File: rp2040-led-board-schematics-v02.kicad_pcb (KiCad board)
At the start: 4 copper layers, 153.7 x 82.5 mm, 117 parts, among them J1 GPIO, J10 LED1Terminal, J11 MainBoard, J12 FrontPanel, J14 ReceiverData, J15 ReceiverRS485, J2 PWR_IN, J3 LED1Terminal, J4 LED1Terminal, J5 LED1Terminal, J6 LED1Terminal, J7 LED1Terminal, J8 LED1Terminal, J9 LED1Terminal, SW1 Button, SW2 PEC16, U1 Pico, U10 MAX485E, U11 LM7805, U12 MAX485E, U14 LM7805, U2 ENC28J60, U3 MAX485E, U4 MAX485E, U5 MAX485E, U6 MAX485E, U7 MAX485E, U8 MAX485E, U9 MAX485E

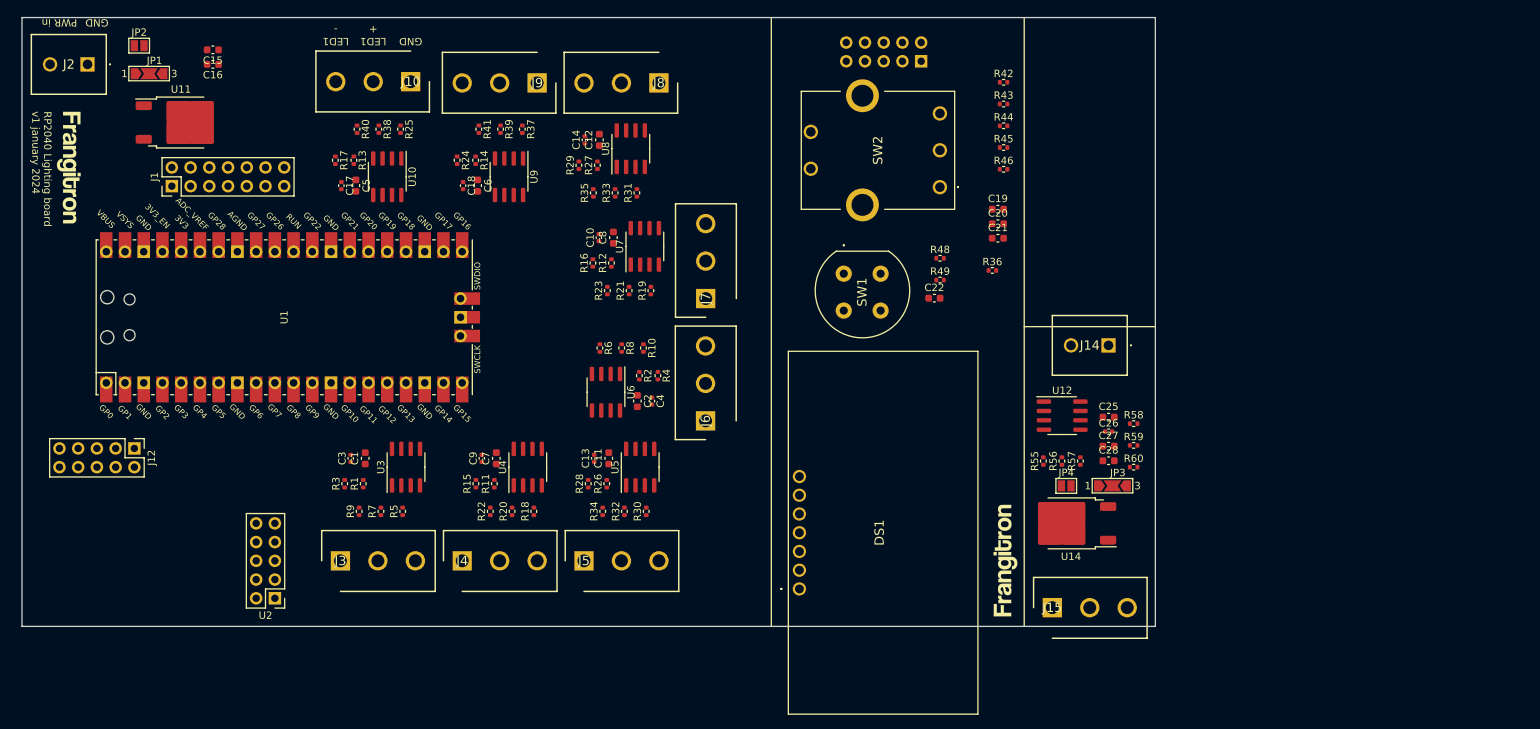
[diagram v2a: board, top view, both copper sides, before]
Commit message: main board PCB done (needs checking)
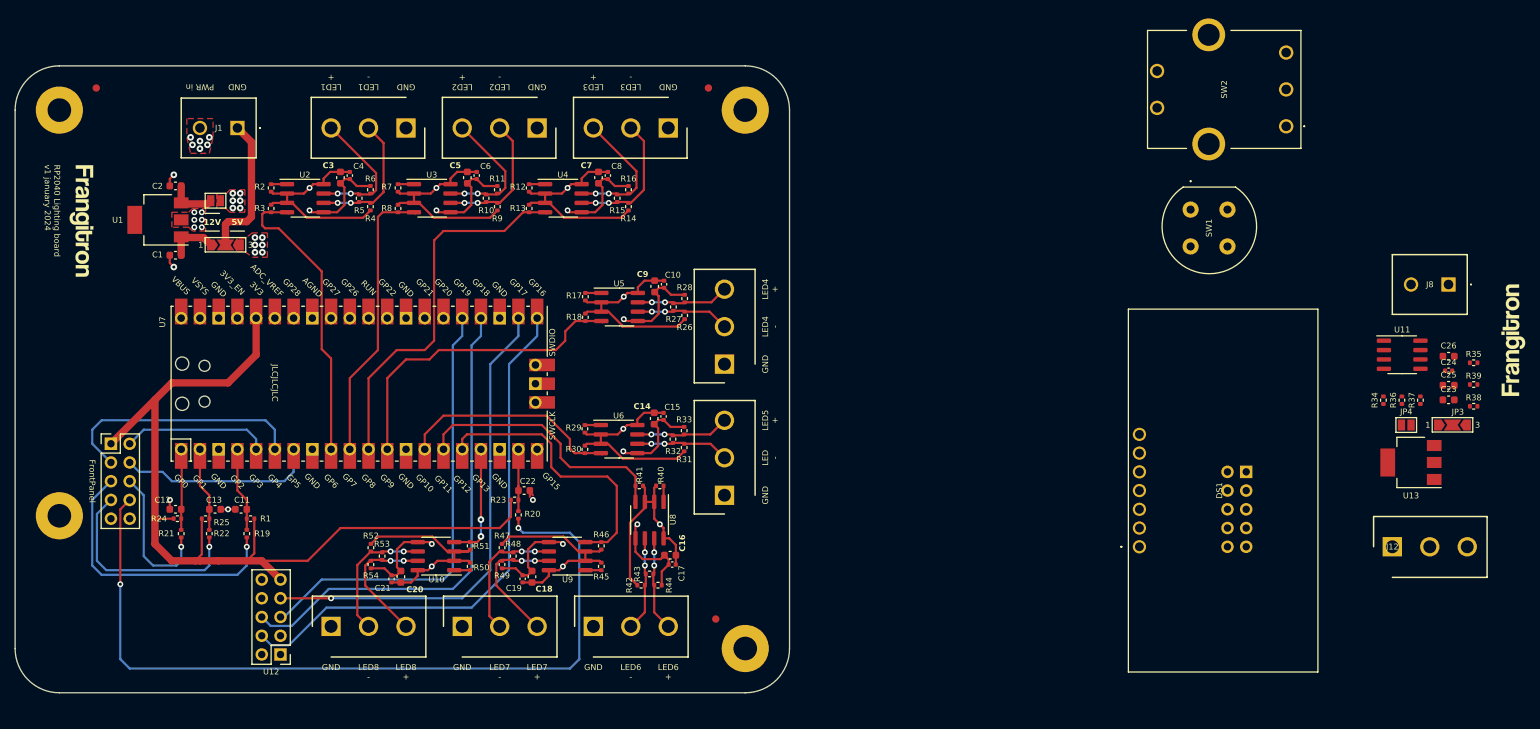
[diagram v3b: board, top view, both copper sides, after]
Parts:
- removed the J1 at (95.2, 67.3)
- removed J10, J3, J4, J6, J7, J9: LED1Terminal, Frangitron:ScrewTerminal_01x03_5.08_Amphenol
- removed the J5 at (151.1, 118.1)
- removed the J8 at (161.3, 53.3)
- removed the U1 at (110.5, 85.1)
- added FM1: Fiducial, Fiducial:Fiducial_1mm_Mask2mm, F.Cu at (85.0, 54.0)
- added FM2: Fiducial, Fiducial:Fiducial_1mm_Mask2mm, F.Cu at (168.0, 54.0)
- added FM3: Fiducial, Fiducial:Fiducial_1mm_Mask2mm, F.Cu at (169.0, 126.0)
- added H1: MountingHole_Pad, MountingHole:MountingHole_3.2mm_M3_Pad, F.Cu at (80.0, 57.0)
- added H2: MountingHole_Pad, MountingHole:MountingHole_3.2mm_M3_Pad, F.Cu at (173.0, 57.0)
- added H4: MountingHole_Pad, MountingHole:MountingHole_3.2mm_M3_Pad, F.Cu at (80.0, 112.0)
- added H5: MountingHole_Pad, MountingHole:MountingHole_3.2mm_M3_Pad, F.Cu at (173.0, 130.0)
- added J14: Terminal, Frangitron:ScrewTerminal_01x03_5.08_Amphenol, F.Cu at (144.8, 59.4)
- added J15: Terminal, Frangitron:ScrewTerminal_01x03_5.08_Amphenol, F.Cu at (162.6, 59.4)
- added J16: Terminal, Frangitron:ScrewTerminal_01x03_5.08_Amphenol, F.Cu at (170.2, 91.4)
- added J17: Terminal, Frangitron:ScrewTerminal_01x03_5.08_Amphenol, F.Cu at (170.2, 109.2)
- added J18: Terminal, Frangitron:ScrewTerminal_01x03_5.08_Amphenol, F.Cu at (152.4, 127.0)
- added J19: Terminal, Frangitron:ScrewTerminal_01x03_5.08_Amphenol, F.Cu at (134.6, 127.0)
- added J2: Terminal, Frangitron:ScrewTerminal_01x03_5.08_Amphenol, F.Cu at (127.0, 59.4)
- added J20: Terminal, Frangitron:ScrewTerminal_01x03_5.08_Amphenol, F.Cu at (116.8, 127.0)
- added U7: Pico, MCU_RaspberryPi_and_Boards:RPi_Pico_SMD_TH, F.Cu at (120.7, 94.1)
- C14: renamed from C9; value 10uF -> 100nF; footprint Capacitor_SMD:C_0402_1005Metric -> Capacitor_SMD:C_0603_1608Metric
- C17: renamed from C7; value 100nF -> 10uF; footprint Capacitor_SMD:C_0603_1608Metric -> Capacitor_SMD:C_0402_1005Metric
- C18: renamed from C4; value 10uF -> 100nF; footprint Capacitor_SMD:C_0402_1005Metric -> Capacitor_SMD:C_0603_1608Metric
- C19: renamed from C2; value 100nF -> 10uF; footprint Capacitor_SMD:C_0603_1608Metric -> Capacitor_SMD:C_0402_1005Metric
- C7: renamed from C10; value 10uF -> 100nF; footprint Capacitor_SMD:C_0402_1005Metric -> Capacitor_SMD:C_0603_1608Metric
- C8: value 100nF -> 10uF; footprint Capacitor_SMD:C_0603_1608Metric -> Capacitor_SMD:C_0402_1005Metric
- R11: renamed from R12; value 10K -> 20K
- R13: renamed from R39; value 20K -> 10K
- R14: renamed from R27; value 10K -> 20K
- R15: renamed from R33; value 20K -> 120
- R18: renamed from R31; value 20K -> 10K
- R2: renamed from R40; value 120 -> 10K
- R22: renamed from R44; value 10k -> 1k
- R25: renamed from R36; value 1k -> 10k
- R27: renamed from R2; value 10K -> 120
- R28: renamed from R23; value 120 -> 20K
- R30: renamed from R8; value 20K -> 10K
- R32: renamed from R6; value 20K -> 120
- R33: renamed from R10; value 120 -> 20K
- R4: renamed from R17; value 10K -> 20K
- R40: renamed from R7; value 20K -> 10K
- R41: renamed from R9; value 120 -> 10K
- R43: renamed from R15; value 10K -> 120
- R44: renamed from R3; value 10K -> 20K
- R45: renamed from R22; value 120 -> 10K
- R47: renamed from R34; value 120 -> 20K
- R48: renamed from R32; value 20K -> 120
- R5: renamed from R25; value 20K -> 120
- R50: renamed from R30; value 20K -> 10K
- R52: renamed from R26; value 10K -> 20K
- R53: renamed from R18; value 20K -> 120
- R54: renamed from R11; value 10K -> 20K
- R6: renamed from R24; value 10K -> 20K
- R7: renamed from R38; value 20K -> 10K
- R9: renamed from R41; value 120 -> 20K
- U1: renamed from U11; footprint Package_TO_SOT_SMD:TO-252-2 -> Package_TO_SOT_SMD:SOT-223
- U13: renamed from U14; footprint Package_TO_SOT_SMD:TO-252-2 -> Package_TO_SOT_SMD:SOT-223
- moved R24 125.3 mm to (96.0, 112.4)
- moved R21 123.2 mm to (96.5, 114.4), turned to -90 degrees
- moved R22 121.1 mm to (100.3, 114.4), turned to -90 degrees
- moved C12 118.0 mm to (95.7, 111.1), turned to 180 degrees
- moved R1 118.0 mm to (105.9, 112.4), turned to 180 degrees
- moved R19 113.9 mm to (105.4, 114.4), turned to 90 degrees
- moved C13 112.3 mm to (101.1, 111.1)
- moved R25 111.9 mm to (99.8, 112.4)
- moved C11 110.4 mm to (104.6, 111.1), turned to 180 degrees
- moved H6 75.1 mm to (277.1, 88.2)
- moved J13 71.0 mm to (240.9, 106.0), turned to 180 degrees
- moved R20 66.9 mm to (142.2, 111.9), turned to -90 degrees
- moved R23 64.9 mm to (141.7, 109.9)
- moved C22 61.4 mm to (143.0, 108.6)
- moved SW1 47.8 mm to (233.4, 70.5)
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- renumbered C15 to C1, C14 to C10, C19 to C11, C20 to C12, C21 to C13, C3 to C15, C1 to C16, C16 to C2, C11 to C20, C13 to C21, C28 to C23, C26 to C24, C27 to C25, C25 to C26, C6 to C3, C17 to C4, C18 to C6, C12 to C9, H1 to H3, H2 to H6, H4 to H7, J2 to J1, J15 to J12, J11 to J13, J12 to J5, J14 to J8, JP2 to JP1, JP1 to JP2, R42 to R1, R35 to R10, R16 to R12, R37 to R16, R29 to R17, R46 to R19, R48 to R20, R45 to R21, R49 to R23, R43 to R24, R19 to R26, R4 to R29, R13 to R3, R21 to R31, R55 to R34, R58 to R35, R56 to R36, R57 to R37, R60 to R38, R59 to R39, R5 to R42, R1 to R46, R20 to R49, R28 to R51, R14 to R8, U5 to U10, U12 to U11, U2 to U12, U10 to U2, U8 to U3, U7 to U4, U9 to U5, U3 to U6, U6 to U8, U4 to U9
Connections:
- C11 pad 1: FPEncoderA -> MCUEncoderS
- C12 pad 1: FPEncoderB -> MCUEncoderA
- C13 pad 1: FPEncoderS -> MCUEncoderB
- C22 pad 1: FPSwitchPush -> MCUSwitchPush
- DS1 pad 1: GND -> FP GND
- DS1 pad 2: +3V3 -> FP +3V3
- DS1 pad 3: +3V3 -> FP +3V3
- DS1 pad 4: GND -> FP GND
- J13 pad 1: +3V3 -> FP +3V3
- J13 pad 10: GND -> FP GND
- J5 pad 2: MBDisplayRST -> MCUDisplayRST
- J5 pad 3: MBDisplaySDA -> MCUDisplaySDA
- J5 pad 4: MBDisplaySCL -> MCUDisplaySCL
- R1 pad 2: FPEncoderA -> MCUEncoderS
- R10 pad 1: Net-(J8-Pin_3) -> /LED to RS486/D+
- R10 pad 2: Net-(J8-Pin_2) (its old number) -> /LED to RS486/D-
- R11 pad 1: +5V -> /LED to RS486/D+
- R11 pad 2: Net-(U7-RO) -> GND
- R12 pad 2: LED5 out -> Net-(U4-RO)
- R13 pad 1: Net-(J9-Pin_3) -> +5V
- R13 pad 2: GND -> LED3 out
- R14 pad 2: Net-(U8-RO) -> /LED to RS487/D-
- R15 pad 1: Net-(J8-Pin_3) -> /LED to RS487/D+
- R15 pad 2: GND -> /LED to RS487/D-
- R16 pad 1: +5V -> /LED to RS487/D+
- R16 pad 2: Net-(J9-Pin_2) -> GND
- R17 pad 2: LED6 out -> Net-(U5-RO)
- R18 pad 2: Net-(J8-Pin_2) (its old number) -> LED4 out
- R19 pad 1: FPEncoderB -> MBEncoderS
- R19 pad 2: Net-(R46-Pad2) -> MCUEncoderS
- R2 pad 1: Net-(J10-Pin_3) -> +5V
- R2 pad 2: Net-(J10-Pin_2) -> Net-(U2-RO)
- R20 pad 1: FPSwitchPush -> MCUSwitchPush
- R20 pad 2: Net-(SW1-K) -> MBSwitchPush
- R21 pad 1: FPEncoderA -> MCUEncoderA
- R21 pad 2: Net-(R45-Pad2) -> MBEncoderA
- R22 pad 1: +3V3 -> MCUEncoderB
- R22 pad 2: FPEncoderS -> MBEncoderB
- R23 pad 2: FPSwitchPush -> MCUSwitchPush
- R24 pad 2: FPEncoderB -> MCUEncoderA
- R25 pad 1: Net-(R36-Pad1) -> +3V3
- R25 pad 2: FPEncoderS -> MCUEncoderB
- R26 pad 2: Net-(J7-Pin_2) -> /LED to RS488/D-
- R27 pad 1: +5V -> /LED to RS488/D+
- R27 pad 2: Net-(U6-RO) -> /LED to RS488/D-
- R28 pad 1: Net-(J7-Pin_3) -> /LED to RS488/D+
- R28 pad 2: Net-(J7-Pin_2) -> GND
- R29 pad 2: LED4 out -> Net-(U6-RO)
- R3 pad 2: Net-(U10-RO) -> LED1 out
- R30 pad 1: Net-(J6-Pin_3) -> +5V
- R30 pad 2: GND -> LED5 out
- R31 pad 1: Net-(J7-Pin_3) -> +5V
- R31 pad 2: GND -> /LED to RS489/D-
- R32 pad 1: +5V -> /LED to RS489/D+
- R32 pad 2: Net-(J6-Pin_2) -> /LED to RS489/D-
- R33 pad 1: Net-(J6-Pin_3) -> /LED to RS489/D+
- R33 pad 2: Net-(J6-Pin_2) -> GND
- R4 pad 2: LED8 out -> /LED to RS485/D-
- R40 pad 1: Net-(J3-Pin_3) -> +5V
- R40 pad 2: GND -> Net-(U8-RO)
- R41 pad 1: Net-(J3-Pin_3) -> +5V
- R41 pad 2: Net-(J3-Pin_2) -> LED6 out
- R42 pad 2: Net-(J3-Pin_2) -> /LED to RS490/D-
- R43 pad 1: +5V -> /LED to RS490/D+
- R43 pad 2: LED2 out -> /LED to RS490/D-
- R44 pad 1: +5V -> /LED to RS490/D+
- R44 pad 2: LED1 out -> GND
- R45 pad 1: Net-(J4-Pin_3) -> +5V
- R45 pad 2: Net-(J4-Pin_2) -> Net-(U9-RO)
- R46 pad 2: Net-(U3-RO) -> LED7 out
- R47 pad 1: Net-(J5-Pin_3) -> +5V
- R47 pad 2: Net-(J5-Pin_2) -> /LED to RS491/D-
- R48 pad 1: Net-(J5-Pin_3) -> /LED to RS491/D+
- R48 pad 2: GND -> /LED to RS491/D-
- R49 pad 1: Net-(J4-Pin_3) -> /LED to RS491/D+
- R5 pad 1: +5V -> /LED to RS485/D+
- R5 pad 2: Net-(J10-Pin_2) -> /LED to RS485/D-
- R50 pad 2: Net-(J5-Pin_2) -> Net-(U10-RO)
- R51 pad 2: LED3 out -> LED8 out
- R52 pad 2: Net-(U5-RO) -> /LED to RS492/D-
- R53 pad 1: +5V -> /LED to RS492/D+
- R53 pad 2: Net-(J4-Pin_2) -> /LED to RS492/D-
- R54 pad 1: +5V -> /LED to RS492/D+
- R54 pad 2: Net-(U4-RO) -> GND
- R6 pad 1: +5V -> /LED to RS485/D+
- R6 pad 2: LED7 out -> GND
- R7 pad 1: Net-(J10-Pin_3) -> +5V
- R7 pad 2: GND -> Net-(U3-RO)
- R8 pad 2: Net-(U9-RO) -> LED2 out
- R9 pad 1: Net-(J9-Pin_3) -> +5V
- R9 pad 2: Net-(J9-Pin_2) -> /LED to RS486/D-
- SW1 pad 2: GND -> FP GND
- SW1 pad 3: Net-(SW1-K) -> FPSwitchPush
- SW2 pad A1: Net-(R45-Pad2) -> FPEncoderA
- SW2 pad B1: Net-(R46-Pad2) -> FPEncoderB
- SW2 pad C1: GND -> FP GND
- SW2 pad D1: Net-(R36-Pad1) -> FPEncoderS
- SW2 pad E1: GND -> FP GND
- U10 pad 1: Net-(U5-RO) -> Net-(U10-RO)
- U10 pad 4: LED3 out -> LED8 out
- U10 pad 6: Net-(J5-Pin_2) -> /LED to RS492/D-
- U10 pad 7: Net-(J5-Pin_3) -> /LED to RS492/D+
- U2 pad 1: Net-(U10-RO) -> Net-(U2-RO)
- U2 pad 4: LED8 out -> LED1 out
- U2 pad 6: Net-(J10-Pin_2) -> /LED to RS485/D-
- U2 pad 7: Net-(J10-Pin_3) -> /LED to RS485/D+
- U3 pad 1: Net-(U8-RO) -> Net-(U3-RO)
- U3 pad 4: LED6 out -> LED2 out
- U3 pad 6: Net-(J8-Pin_2) (its old number) -> /LED to RS486/D-
- U3 pad 7: Net-(J8-Pin_3) -> /LED to RS486/D+
- U4 pad 1: Net-(U7-RO) -> Net-(U4-RO)
- U4 pad 4: LED5 out -> LED3 out
- U4 pad 6: Net-(J7-Pin_2) -> /LED to RS487/D-
- U4 pad 7: Net-(J7-Pin_3) -> /LED to RS487/D+
- U5 pad 1: Net-(U9-RO) -> Net-(U5-RO)
- U5 pad 4: LED7 out -> LED4 out
- U5 pad 6: Net-(J9-Pin_2) -> /LED to RS488/D-
- U5 pad 7: Net-(J9-Pin_3) -> /LED to RS488/D+
- U6 pad 1: Net-(U3-RO) -> Net-(U6-RO)
- U6 pad 4: LED1 out -> LED5 out
- U6 pad 6: Net-(J3-Pin_2) -> /LED to RS489/D-
- U6 pad 7: Net-(J3-Pin_3) -> /LED to RS489/D+
- U8 pad 1: Net-(U6-RO) -> Net-(U8-RO)
- U8 pad 4: LED4 out -> LED6 out
- U8 pad 6: Net-(J6-Pin_2) -> /LED to RS490/D-
- U8 pad 7: Net-(J6-Pin_3) -> /LED to RS490/D+
- U9 pad 1: Net-(U4-RO) -> Net-(U9-RO)
- U9 pad 4: LED2 out -> LED7 out
- U9 pad 6: Net-(J4-Pin_2) -> /LED to RS491/D-
- U9 pad 7: Net-(J4-Pin_3) -> /LED to RS491/D+
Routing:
- net +5V: track 0.00 -> 232.3 mm, vias 0 -> 20
- net +3V3: track 0.00 -> 121.5 mm
- net GND: track 0.00 -> 113.0 mm, vias 0 -> 25
- net MBSwitchPush: track 0.00 -> 111.6 mm, vias 0 -> 2
- net PI spi0 RX: track 0.00 -> 74.0 mm
- net PI spi0 SCK: track 0.00 -> 66.8 mm
- net PI spi0 CSn: track 0.00 -> 65.8 mm, vias 0 -> 1
- net PI spi0 TX: track 0.00 -> 60.7 mm
- net LED3 out: track 0.00 -> 51.1 mm
- net LED4 out: track 0.00 -> 42.9 mm
- net LED1 out: track 0.00 -> 40.6 mm
- net LED7 out: track 0.00 -> 38.8 mm
- net LED2 out: track 0.00 -> 38.5 mm
- net MBEncoderS: track 0.00 -> 38.3 mm, vias 0 -> 1
- net LED6 out: track 0.00 -> 36.3 mm
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- added copper zone on F.Cu, net +5V
- added copper zone on In2.Cu, net +5V
- added copper zone on F.Cu, net GND
- added copper zone on In1.Cu, net GND
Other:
- board size 153.7 x 82.5 mm -> 105 x 85 mm
- board text added: "12V"
- board text added: "5V"
- board text added: "JLCJLCJLC"
- board text added: "LED -"
- board text added: "LED2 +"
- board text added: "LED2 -"
- board text added: "LED3 +"
- board text added: "LED3 -"
- board text added: "LED4 +"
- board text added: "LED4 -"
- board text added: "LED5 +"
- board text added: "LED6 +"
- board text added: "LED6 -"
- board text added: "LED7 +"
- board text added: "LED7 -"
- board text added: "LED8 +"
- board text added: "LED8 -"

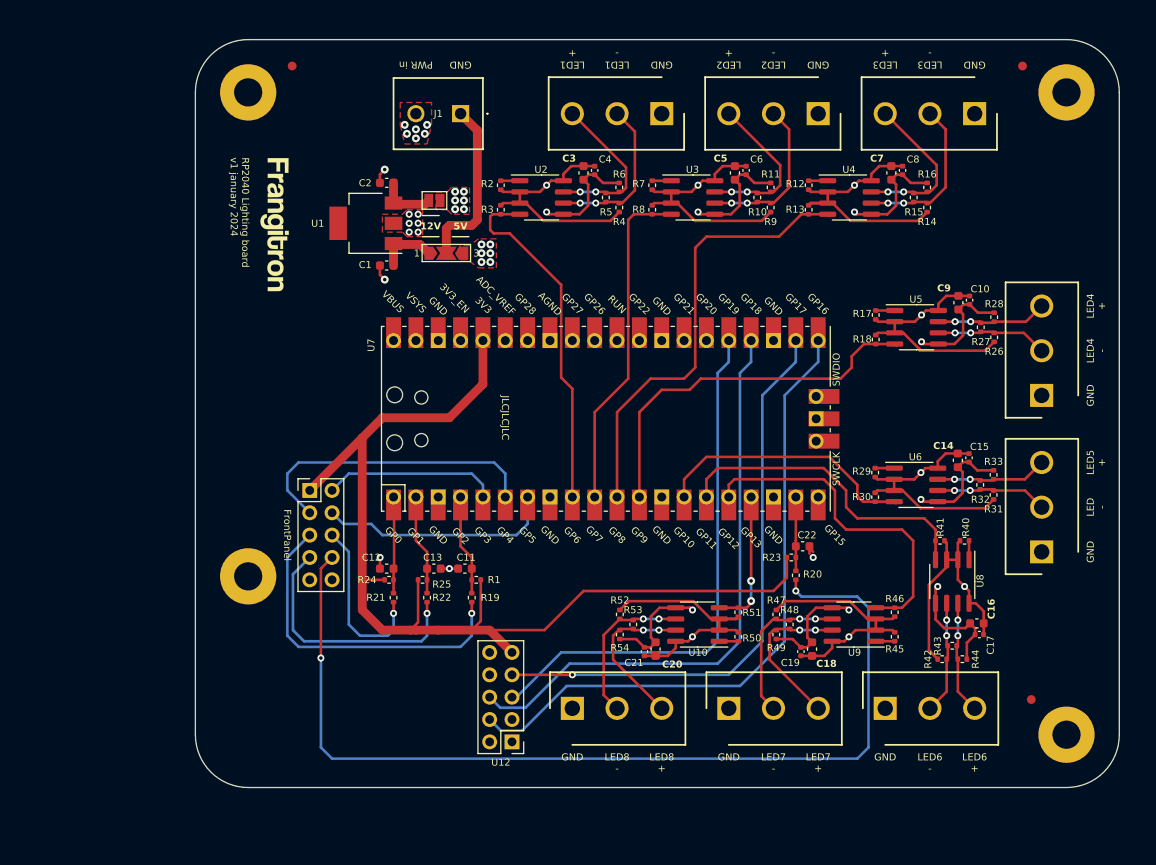
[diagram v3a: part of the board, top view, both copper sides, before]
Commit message: fix ENC module dimensions + adapt pcb accordingly
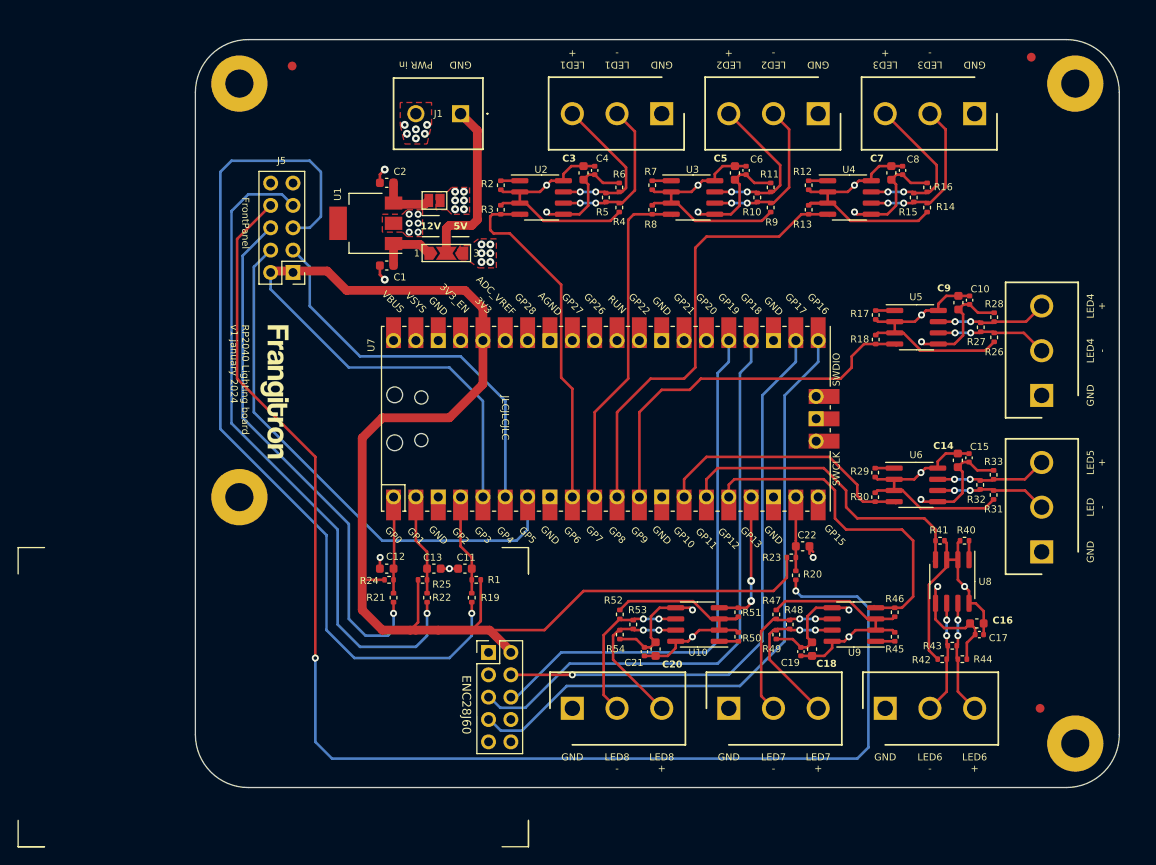
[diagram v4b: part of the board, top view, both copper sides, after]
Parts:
- U12: footprint Frangitron:ENC28J60_module -> Library:ENC28J60-SPI-Ethernet-Module
- moved J5 24.8 mm to (85.1, 77.5), turned to 180 degrees
- moved H3 19.0 mm to (83.0, 91.0)
- moved H4 9.06 mm to (79.0, 103.0)
- moved U12 9.04 mm to (109.9, 125.7), turned to 0 degrees
- moved FM2 1.41 mm to (169.0, 53.0)
- moved FM3 1.41 mm to (170.0, 127.0)
- moved H1 1.41 mm to (79.0, 56.0)
- moved H2 1.41 mm to (174.0, 56.0)
- moved H5 1.41 mm to (174.0, 131.0)
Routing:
- net MBEncoderS: track 38.3 -> 101.0 mm
- net MBEncoderB: track 28.9 -> 75.8 mm
- net MBSwitchPush: track 111.6 -> 156.6 mm
- net MBEncoderA: track 20.0 -> 60.1 mm
- net MCUDisplaySCL: track 26.9 -> 60.6 mm
- net MCUDisplayRST: track 19.8 -> 42.2 mm
- net +3V3: track 121.5 -> 142.3 mm
- net MCUDisplaySDA: track 34.0 -> 44.7 mm

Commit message: 1st panel test, before cloning 8 receivers
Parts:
- added H10: ~, Library:mouse-bites-1x07-jlc, F.Cu at (225.0, 93.0)
- added H11: ~, Library:mouse-bites-1x07-jlc, F.Cu at (225.0, 95.0)
- added H8: MountingHole_Pad, MountingHole:MountingHole_3.2mm_M3_Pad, F.Cu at (197.0, 56.0)
- added H9: MountingHole_Pad, MountingHole:MountingHole_3.2mm_M3_Pad, F.Cu at (197.0, 131.0)
- JP3: value 1-2 12V -> 12V
- JP4: value 12V -> 1-2 12V
- moved H6 55.2 mm to (232.0, 120.0)
- moved J13 48.0 mm to (193.0, 102.2), turned to -90 degrees
- moved J8 44.4 mm to (227.5, 98.0)
- moved JP3 44.2 mm to (228.6, 117.9)
- moved R34 44.2 mm to (219.3, 114.6)
- moved R35 44.2 mm to (231.5, 109.5)
- moved R39 44.2 mm to (231.5, 112.4)
- moved R38 44.2 mm to (231.5, 115.4)
- moved U13 44.2 mm to (223.0, 123.0)
- moved C23 44.2 mm to (228.1, 114.5)
- moved C24 44.2 mm to (228.1, 110.6)
- moved C25 44.2 mm to (228.1, 112.5)
- moved C26 44.2 mm to (228.1, 108.6)
- moved R36 44.2 mm to (221.8, 114.6)
- moved R37 44.2 mm to (224.3, 114.6)
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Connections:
- net Recv5 GND renamed Recv GND
- C23 pad 1: Net-(JP4-B) -> Net-(JP3-B)
- C24 pad 1: Recv5 +5V -> Recv +5V
- C25 pad 1: Net-(JP3-A) -> Net-(JP4-A)
- C26 pad 1: Recv5 +5V -> Recv +5V
- J12 pad 1: Net-(J12-Pin_1) -> Recv PWR
- JP3 pad 1: Net-(JP3-A) -> Recv +5V
- JP3 pad 2: Net-(J12-Pin_1) -> Net-(JP3-B)
- JP3 pad 3: Recv5 +5V -> (no net)
- JP4 pad 1: Recv5 +5V -> Net-(JP4-A)
- JP4 pad 2: Net-(JP4-B) -> Recv PWR
- R34 pad 1: Recv5 +5V -> Recv +5V
- R35 pad 1: Recv5 +5V -> Recv +5V
- R36 pad 1: Recv5 +5V -> Recv +5V
- R37 pad 1: Recv5 +5V -> Recv +5V
- U11 pad 8: Recv5 +5V -> Recv +5V
- U13 pad 1: Net-(JP3-A) -> Net-(JP4-A)
- U13 pad 3: Net-(JP4-B) -> Net-(JP3-B)
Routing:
- net GND: track 113.0 -> 111.0 mm
- net +3V3: track 142.3 -> 140.3 mm
- net PI spi0 CSn: track 65.8 -> 66.3 mm
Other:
- board size 105 x 85 mm -> 161 x 99 mm
- board text added: "<-- V-CUT"
- board text added: "V-CUT -->"
